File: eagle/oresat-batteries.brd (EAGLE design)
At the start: 99.8 x 94.6 mm, 312 parts, among them J1 J-SAMTEC-TFM-120-X1-XXX-D-RA, J4 ORESAT-DEBUG-CONNECTOR-ALL, Q1 DMP2240UDM, Q10 NTR4101, Q11 PMV45EN, Q12 Si7625DN, Q13 Si7625DN, Q14 NTR4101, Q15 NTR4101, Q16 Si7625DN, Q17 Si7625DN, Q18 Si7625DN, Q19 Si7625DN, Q2 PMV45EN, Q22 PMV45EN, Q23 NTR4101, Q24 PM45VEN, Q25 PM45VEN, Q26 PM45VEN, Q27 PM45VEN, Q28 NTR4101, Q29 PM45VEN, Q3 DMP3050LVT-7, Q30 Si7625DN, Q31 Si7625DN, Q32 NTR4101, Q33 NTR4101, Q34 Si7625DN, Q35 Si7625DN, Q36 Si7625DN, Q37 Si7625DN, Q4 DMP3050LVT-7, Q40 PM45VEN, Q41 NTR4101, Q42 DMP2240UDM, Q43 DMP2240UDM, Q44 PMV45EN, Q45 FDMQ86530L_2-GATES, Q5 PMV45EN, Q6 PM45VEN, Q7 PM45VEN, Q8 PM45VEN, Q9 PM45VEN, U1 MAX7310ATE, U10 LTC4412, U11 LTC4412, U12 MAX17205G, U13 S-8209AAA-T8T1U, U14 S-8209AAA-T8T1U, U15 LTC4412, U16 LTC4412, U17 MAX17205G, U2 MIC842LYC5, U20 TCAN330, U21 STM32F091C, U3 MIC842LYC5, U4 MAX4211FETE, U5 TPS62111RSA, U8 S-8209AAA-T8T1U, U9 S-8209AAA-T8T1U, X3 16MHZ-2.5x2mm

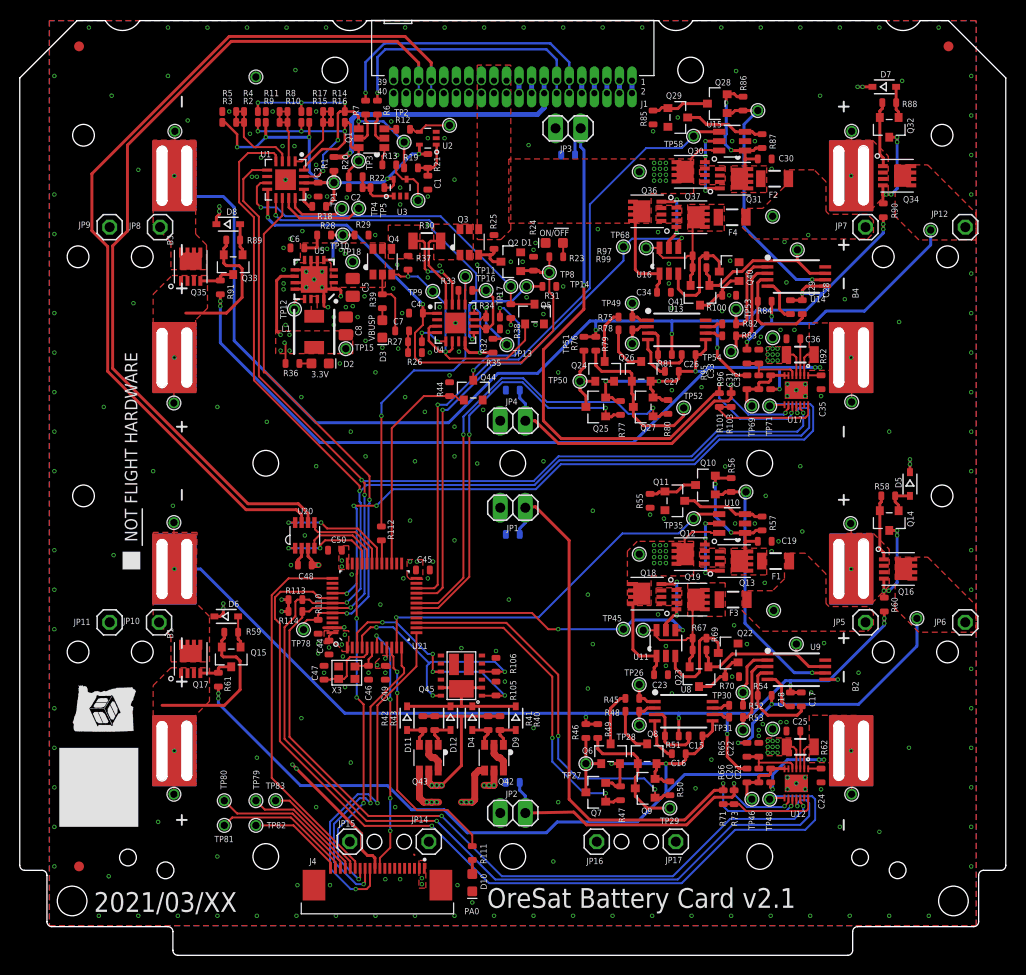
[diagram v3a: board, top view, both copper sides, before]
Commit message: OreSat Battery Card v2.1
- Shrunk fastener foot prints to gain more room.
- Redid DF3 switch layouts to get the jumper wires closer to the switche's mini-contact holes.
- Added fiducials.
- Replaced quad N channel MOSFET with four N channels because the quad pack is unobtainium right now.
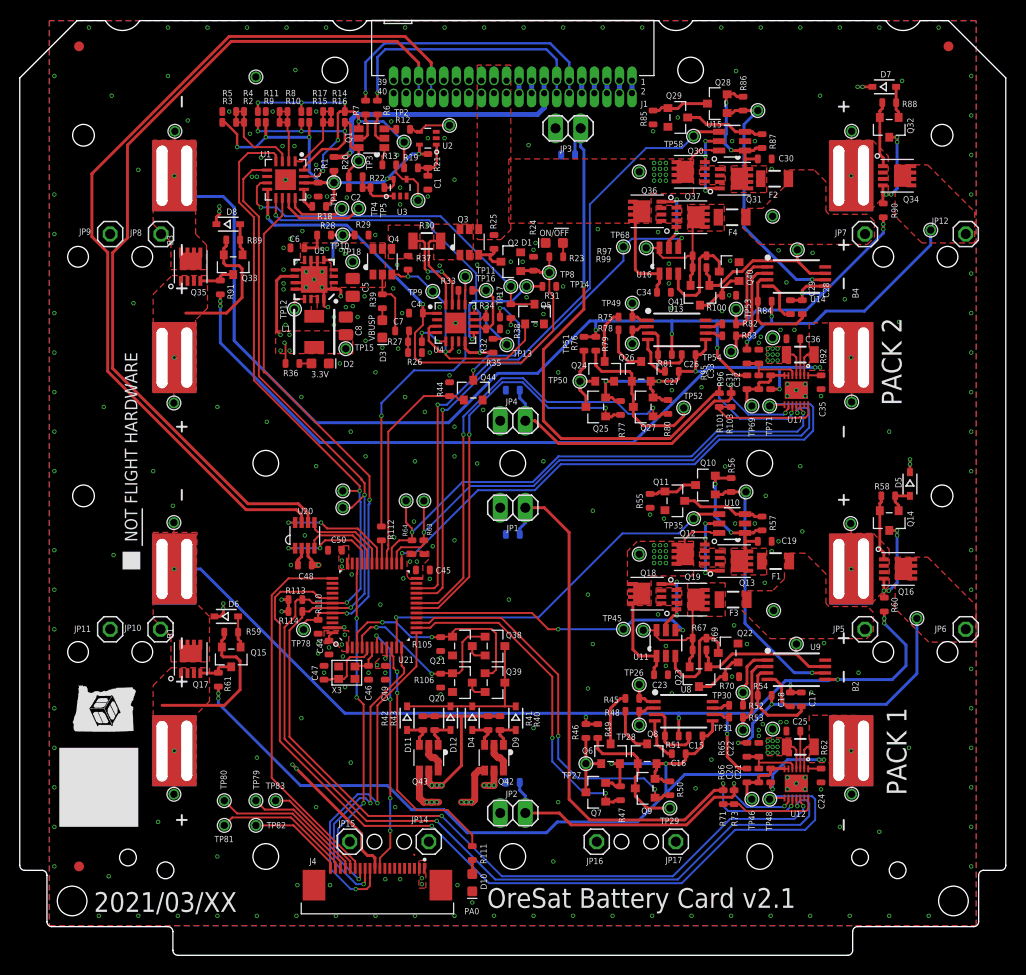
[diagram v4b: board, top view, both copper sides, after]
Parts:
- removed Q45: FDMQ86530L_2-GATES, Q-On_Semiconductor-FDMQ86530L-MOSFET-4-N-CH:FDMQ8203
- added Q20, Q21, Q38, Q39: PMV45EN, Q-MOSFET-NCH-SOT23-3:SOT23-3
- added R63, R64: 4.7k, oresat-rcl:.0603-C-NOSILK
- added TP19, TP20, TP21, TP22: TEST-POINT-LARGE-SQUARE, oresat-misc:1X01
- moved R105 7.18 mm to (42.6, 31.5), turned to 270 degrees
- moved R106 5.82 mm to (42.6, 27.8), turned to 270 degrees
- moved JP10 0.72 mm to (14.2, 33.0)
- moved JP8 0.71 mm to (14.3, 73.0)
- moved JP11 0.70 mm to (9.15, 33.0)
- moved JP9 0.70 mm to (9.15, 73.0)
- moved JP12 0.70 mm to (95.8, 73.0)
- moved JP5 0.70 mm to (85.5, 33.0)
- moved JP6 0.70 mm to (95.8, 33.0)
- moved JP7 0.70 mm to (85.5, 73.0)
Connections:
- new net I2C2_SCL: R63.1, TP19.1, U17.11, U21.26
- new net I2C2_SDA: R64.1, TP20.1, U17.12, U21.27
- new net N$88: Q20.3, Q39.2
- new net N$92: Q21.3, Q38.2
- net 3.3V: now also R63.2, R64.2
- net ALERTA-PK2: now also U21.25; no longer U21.40
- net GND: now also Q20.2, Q21.2; no longer Q45.5, Q45.6, Q45.7, Q45.8
- net HEATER-ON-1: now also Q21.1, Q39.1; no longer Q45.1, Q45.9
- net HEATER-ON-2: now also Q20.1, Q38.1; no longer Q45.12, Q45.4
- net MOARPWR: now also U21.28; no longer U21.27
- net N$64: now also Q38.3, Q39.3; no longer Q45.11, Q45.13, Q45.2
- net PB6/SCL: now also TP21.1; no longer U17.11
- net PB7/SDA: now also TP22.1; no longer U17.12
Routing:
- net I2C2_SCL: track 0.00 -> 56.4 mm, vias 0 -> 2
- net I2C2_SDA: track 0.00 -> 54.5 mm, vias 0 -> 2
- net PB6/SCL: track 193.2 -> 142.2 mm, vias 5 -> 4
- net PB7/SDA: track 181.4 -> 134.8 mm, vias 6 -> 4
- net ALERTA-PK2: track 69.1 -> 56.4 mm, vias 3 -> 1
- net HEATER-ON-2: track 24.8 -> 19.1 mm, vias 3 -> 2
- net INTERCELL-PK1: track 104.1 -> 108.8 mm
- net N$88: track 0.00 -> 2.10 mm
- net N$92: track 0.00 -> 2.10 mm
- net HEATER-ON-1: track 24.2 -> 22.3 mm, vias 4 -> 2
- net VBATT-POS-PK1: track 27.5 -> 29.2 mm
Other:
- board text added: "PACK 1"
- board text added: "PACK 2"

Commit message: Battery v3.0. Might actually work, and with less dropouts.
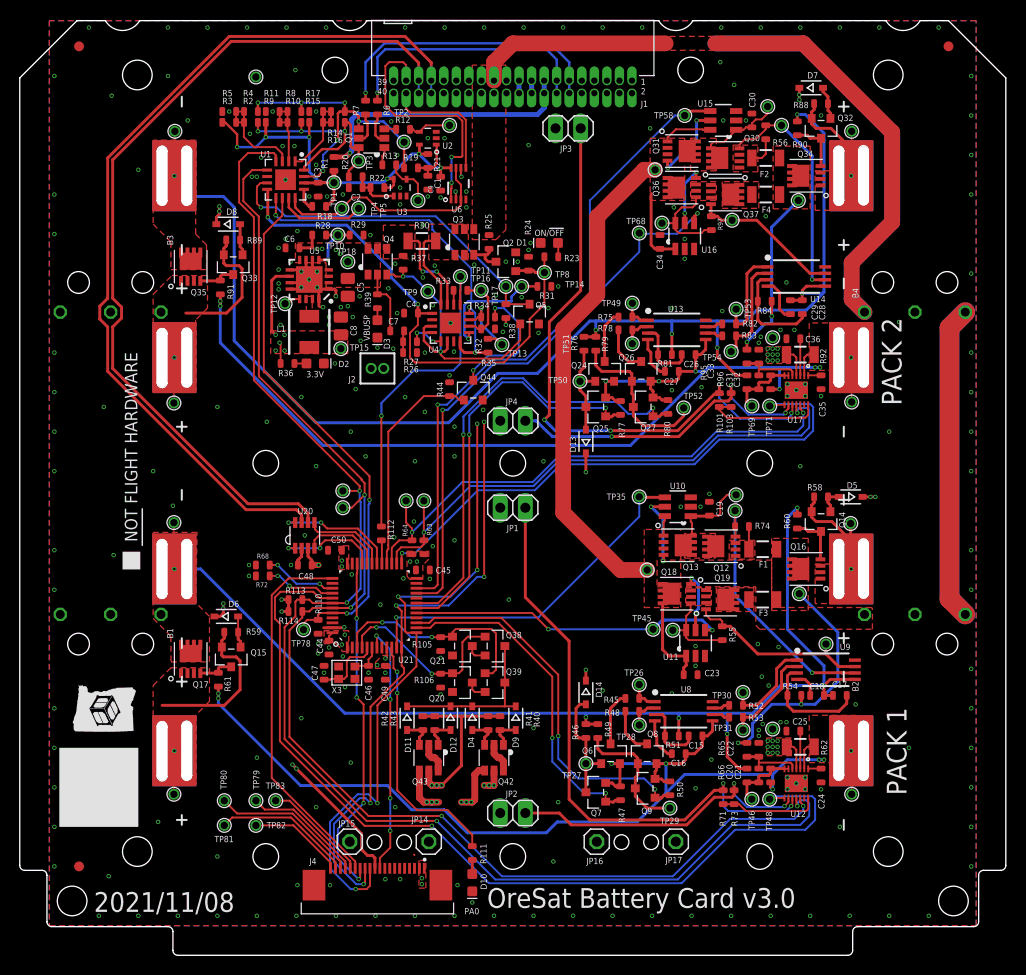
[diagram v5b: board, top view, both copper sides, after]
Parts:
- removed JP10, JP11, JP12, JP5, JP6, JP7, JP8, JP9: (no value), pinhead:1X01
- removed PCB1: ORESAT-CARD-V1.3-BATTERY, oresat-cards:ORESAT-CARD-V1.3-BATTERY
- removed Q10, Q23, Q28, Q41: NTR4101, Q-MOSFET-PCH-SOT23-3:SOT23-3
- removed Q11, Q22: PMV45EN, Q-MOSFET-NCH-SOT23-3:SOT23-3
- removed Q29, Q40: PM45VEN, Q-MOSFET-NCH-SOT23-3:SOT23-3
- removed R100, R57, R67, R69, R70, R85, R86, R87, R99: 100k, oresat-rcl:.0603-C-NOSILK
- removed R102, R104: NP, oresat-rcl:.0603-C-NOSILK
- removed TP37, TP60: TEST-POINT-LARGE-SQUARE, oresat-misc:1X01
- added C9: 100n, oresat-rcl:.0603-C-NOSILK
- added D13, D14: 1N4151WS, D-Generic-silicon-SOD-323:SOD323-R
- added J2: FTS-102-01-X-SJ, J-Samtec-FTS-102-01-1.27mm-th:SAMTEC-FTS-102-01-X-S
- added R68: 10k, oresat-rcl:.0603-C-NOSILK
- added SW1, SW3: OMRON-D2F-5L3-LEFT, SW-Omron-D2F-L3-D-switch:D2F-L3-D-HORIZONTAL-L
- added SW2, SW4: OMRON-D2F-5L3-RIGHT, SW-Omron-D2F-L3-D-switch:D2F-L3-D-HORIZONTAL-R
- added TP23, TP24: TEST-POINT-LARGE-SQUARE, oresat-misc:1X01
- added U$2: (no value), oresat-cards:ORESAT-CARD-V1.3-BATTERY-V3.0
- added U6: TS5A21366DCUR, U-TI-TS5A21366-2xSPST-analog-switch:DCU0008A_N
- R72: value NP -> 10k
- R74: value NP -> 100k
- moved R56 35.9 mm to (75.5, 83.3), turned to 270 degrees
- moved R74 34.8 mm to (73.1, 43.4), flipped to the top
- moved R72 25.6 mm to (24.6, 38.4), flipped to the top
- moved R55 15.3 mm to (71.1, 32.6), turned to 270 degrees
- moved TP61 13.7 mm to (78.8, 76.4)
- moved R60 12.2 mm to (78.7, 43.9), turned to 90 degrees
- moved TP38 12.2 mm to (78.9, 36.6)
- moved R90 12.0 mm to (78.7, 83.7), turned to 90 degrees
- moved Q16 9.30 mm to (79.6, 39.1), turned to 90 degrees
- moved Q34 9.20 mm to (79.6, 78.9), turned to 90 degrees
- moved D7 7.40 mm to (80.1, 87.8)
- moved TP56 7.25 mm to (72.1, 74.4)
- moved Q14 6.90 mm to (81.1, 43.9)
- moved Q32 6.90 mm to (81.1, 83.7)
- moved R88 6.90 mm to (81.1, 86.2)
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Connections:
- removed net N$41: F3.1, Q19.5, Q19.6, Q19.7, Q19.8, Q19.PAD, Q23.2, R67.2, R69.2, TP44.1, U11.6
- removed net N$44: Q18.1, Q18.2, Q18.3, Q19.1, Q19.2, Q19.3
- removed net N$76: Q30.1, Q30.2, Q30.3, Q31.1, Q31.2, Q31.3
- removed net N$81: Q36.1, Q36.2, Q36.3, Q37.1, Q37.2, Q37.3
- removed net N$89: F4.1, Q37.5, Q37.6, Q37.7, Q37.8, Q37.PAD, Q41.2, R97.2, R99.2, TP67.1, U16.6
- removed net N$93: Q28.3, Q29.1, R85.2
- removed net N$94: Q40.3, R97.1, U16.3
- removed net N$95: Q40.1, Q41.3, R100.2
- removed net NLEKJRWER: Q11.3, R57.1, U10.3
- removed net NLEKJRWER2: Q29.3, R87.1, U15.3
- removed net SPARE1: J1.10, J1.9
- removed net SPARE2: J1.7, J1.8
- removed net SPARE3: J1.5, J1.6
- removed net SPARE4: J1.3, J1.4
- removed net SPARE5: J1.1, J1.2
- removed net VBATT-POS-PK1: JP6.1, Q16.5, Q16.6, Q16.7, Q16.8, Q16.PAD, R54.2, R65.2, TP38.1
- removed net VBATT-POS-PK2: JP12.1, Q34.5, Q34.6, Q34.7, Q34.8, Q34.PAD, R84.2, R95.2, TP61.1
- removed net VBATT-SW-PK1: F1.2, F3.2, JP5.1, TP37.1
- removed net VBATT-SW-PK2: F2.2, F4.2, JP7.1, TP60.1
- new net C3-UART-RX: J1.38, U6.5
- new net C3-UART-TX: J1.37, U6.1
- new net INTERSW: SW3.C, SW4.C
- new net N$1: U21.45
- new net N$100: F1.1, Q12.1, Q12.2, Q12.3, R74.1
- new net N$109: Q18.1, Q18.2, Q18.3, Q19.1, Q19.2, Q19.3, R55.2, TP44.1, U11.6
- new net N$13: U21.46
- new net N$54: R68.1, U21.39
- new net N$99: R72.1, U21.40
- new net VBAT: C23.1, C34.1, Q13.1, Q13.2, Q13.3, Q18.5, Q18.6, Q18.7, Q18.8, Q18.PAD, Q31.1, Q31.2, Q31.3, Q36.5, Q36.6, Q36.7, Q36.8, Q36.PAD, SW4.NC, TP36.1, TP59.1, U10.6, U11.1, U15.6, U16.1
- new net VBATT-PK1: F1.2, F3.2, Q16.5, Q16.6, Q16.7, Q16.8, Q16.PAD, R54.2, R65.2, TP38.1
- new net VBATT-PK2: F2.2, F4.2, Q34.5, Q34.6, Q34.7, Q34.8, Q34.PAD, R84.2, R95.2, TP61.1
- net !CHARGE-PK1: now also Q19.4, R55.1; no longer Q23.1, R69.1
- net !CHARGE-PK2: now also Q37.4, R97.1; no longer Q41.1, R99.1
- net !DISCHARGE-PK1: now also Q12.4, R74.2; no longer Q10.1, R56.1
- net !DISCHARGE-PK2: now also Q30.4, R56.1; no longer Q28.1, R86.1
- net !SD: now also D13.C, D14.C, SW1.NO, SW2.NO; no longer JP10.1, JP8.1
- net 3.3V: now also J2.1
- net AIN1-PK1: no longer R74.2
- net AIN1-PK2: no longer R104.2
- net AIN2-PK1: no longer R72.2
- net AIN2-PK2: no longer R102.2
- net GND: now also C9.1, R68.2, R72.2, SW1.C, SW2.C, U15.3, U16.3, U6.4; no longer J1.31, J1.32, J1.37, J1.38, JP11.1, JP9.1, Q11.2, Q22.2, Q29.2, Q40.2, R100.1, R102.1, R104.1, R55.1, R70.1, R72.1, R74.1, R85.1
- net N$22: now also Q36.1, Q36.2, Q36.3, Q37.1, Q37.2, Q37.3, R97.2, TP67.1, U16.6; no longer Q22.3, R67.1, U11.3
- net N$43: no longer Q19.4
- net N$48: now also F3.1, Q19.5, Q19.6, Q19.7, Q19.8, Q19.PAD; no longer Q10.3, Q11.1, R55.2
- net N$51: now also D14.A
- net N$56: now also F2.1, Q30.1, Q30.2, Q30.3, R56.2; no longer Q22.1, Q23.3, R70.2
- net N$60: now also U6.3, U6.7
- net N$74: no longer Q30.4
- net N$8: no longer Q12.4
- net N$80: no longer Q37.4
- net N$9: now also F4.1, Q37.5, Q37.6, Q37.7, Q37.8, Q37.PAD; no longer Q12.1, Q12.2, Q12.3, Q13.1, Q13.2, Q13.3
- net N$91: now also D13.A
- net PA2/USART2_TX: now also U6.6
- net PA3/USART2_RX: now also U6.2
- net VBATT-F-PK1: now also Q12.5, Q12.6, Q12.7, Q12.8, Q12.PAD, TP23.1; no longer F1.1, Q10.2, R56.2, R57.2
- net VBATT-F-PK2: now also Q30.5, Q30.6, Q30.7, Q30.8, Q30.PAD, TP24.1; no longer F2.1, Q28.2, R86.2, R87.2
- net VBUS: now also SW3.NC; no longer C23.1, C34.1, J1.21, J1.22, Q12.5, Q12.6, Q12.7, Q12.8, Q12.PAD, Q18.5, Q18.6, Q18.7, Q18.8, Q18.PAD, Q30.5, Q30.6, Q30.7, Q30.8, Q30.PAD, Q36.5, Q36.6, Q36.7, Q36.8, Q36.PAD, TP36.1, TP59.1, U10.6, U11.1, U15.6, U16.1
- net VPD: now also C9.2, J2.2, U6.8
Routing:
- net INTERSW: track 0.00 -> 95.8 mm
- net VBUS: track 29.6 -> 104.2 mm, vias 24 -> 0
- net VBAT: track 0.00 -> 74.4 mm
- net !SD: track 208.5 -> 278.1 mm, vias 8 -> 10
- net PA2/USART2_TX: track 31.7 -> 91.3 mm, vias 2 -> 6
- net PA3/USART2_RX: track 36.7 -> 94.7 mm, vias 2 -> 6
- net VBATT-POS-PK1: track 29.2 -> 0.00 mm, vias 2 -> 0
- net VBATT-POS-PK2: track 27.2 -> 0.00 mm, vias 2 -> 0
- net VBATT-PK1: track 0.00 -> 25.7 mm, vias 0 -> 2
- net C3-UART-TX: track 0.00 -> 25.4 mm, vias 0 -> 2
- net VBATT-PK2: track 0.00 -> 19.9 mm, vias 0 -> 2
- net N$60: track 6.20 -> 23.4 mm
- net VPD: track 69.9 -> 85.8 mm, vias 6 -> 7
- net N$41: track 13.1 -> 0.00 mm
- net C3-UART-RX: track 0.00 -> 12.9 mm
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- added copper zone on layer 1, net N$100
- added copper zone on layer 1, net N$109
- added copper zone on layer 1, net N$22
- added copper zone on layer 1, net N$48
- added copper zone on layer 1, net N$56
- added copper zone on layer 1, net VBAT
- added copper zone on layer 1, net VBATT-PK1
- added copper zone on layer 1, net VBATT-PK2
- removed copper zone on layer 1, net N$41
- removed copper zone on layer 1, net N$44
- removed copper zone on layer 1, net N$76
- removed copper zone on layer 1, net N$81
- removed copper zone on layer 1, net N$89
- removed copper zone on layer 1, net VBATT-POS-PK1
- removed copper zone on layer 1, net VBATT-POS-PK2
- removed copper zone on layer 1, net VBATT-SW-PK1
- removed copper zone on layer 1, net VBATT-SW-PK2
- removed copper zone on layer 15, net VBUS
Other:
- board text added: "2021/11/08"
- board text added: "OreSat Battery Card v3.0"
- board text removed: "2021/03/XX"
- board text removed: "OreSat Battery Card v2.1"

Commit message: v3.0 sent off to fab! Updated BOM, and committed final changes to card. Lots of small changes, including better power routing, resistors in the UART line to the C3, and as mentioned in an earlier commit, making the charge/discharge switch independent of the ideal diodes.
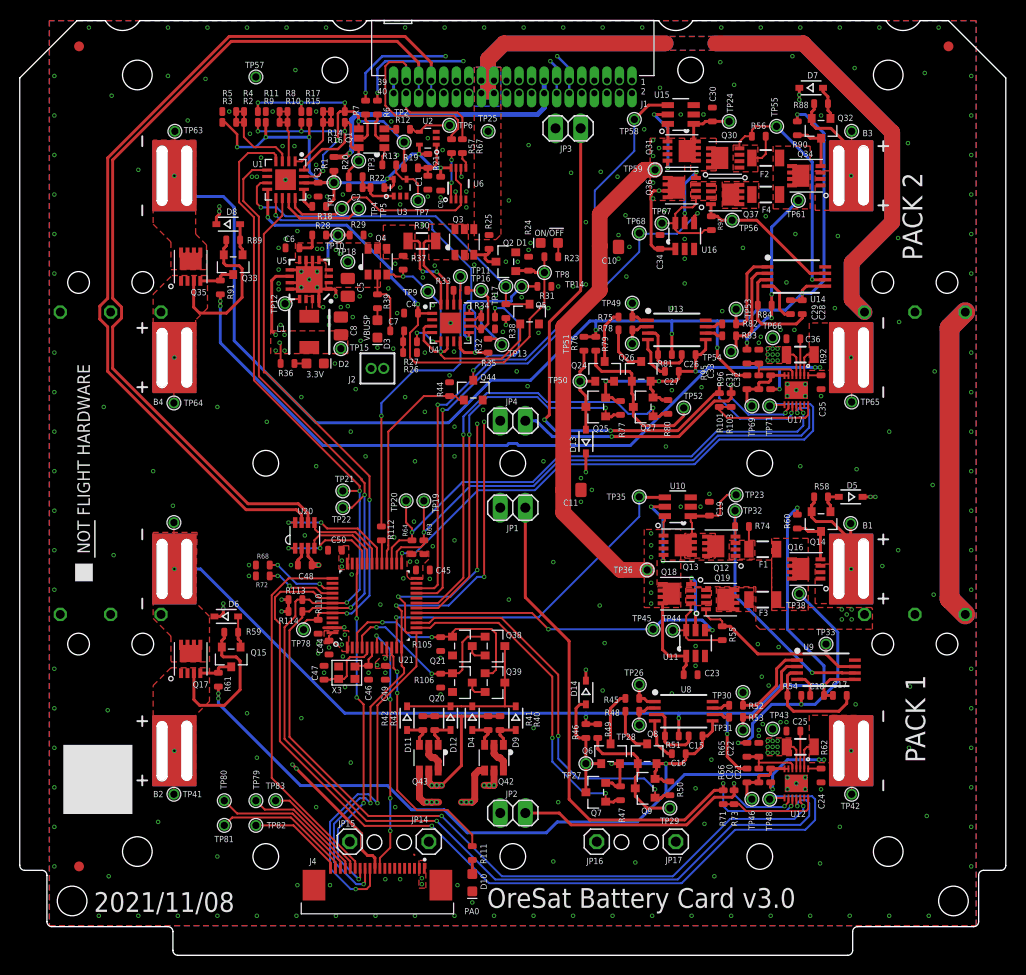
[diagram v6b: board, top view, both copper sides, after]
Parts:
- added C10, C11: 10u, oresat-rcl:.0805-B-NOSILK
- added R57, R67: 10k, oresat-rcl:.0603-C-NOSILK
- added TP25: TEST-POINT-LARGE-SQUARE, oresat-misc:1X01
- R11, R17, R5: value NP -> 10k
- moved SW3 36.6 mm to (90.6, 31.5), turned to 180 degrees
- moved SW4 36.6 mm to (90.6, 68.1), turned to 0 degrees
- moved TP58 5.12 mm to (62.2, 84.6)
- moved U$1 4.95 mm to (7.10, 38.1)
- moved U15 4.34 mm to (66.9, 85.1)
- moved TP24 4.18 mm to (71.8, 84.4)
- moved C30 4.04 mm to (70.1, 85.1)
- moved R56 0.81 mm to (74.8, 82.9), turned to 0 degrees
- moved TP55 0.51 mm to (76.6, 83.9)
- moved R84 0.40 mm to (75.4, 65.8)
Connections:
- removed net CAN2_H: J1.17, J1.18
- removed net CAN2_L: J1.19, J1.20
- net C3-UART-RX: now also R67.2; no longer U6.5
- net C3-UART-TX: now also R57.2; no longer U6.1
- net GND: now also C10.2, C11.2, U10.3, U11.3
- net INTERSW: now also SW3.NC, SW4.NC; no longer SW3.C, SW4.C
- net N$1: now also R57.1, U6.1; no longer U21.45
- net N$13: now also R67.1, U6.5; no longer U21.46
- net VBAT: now also C10.1, C11.1, SW3.C; no longer SW4.NC
- net VBUS: now also SW4.C, TP25.1; no longer SW3.NC
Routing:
- net VBAT: track 74.4 -> 147.5 mm, vias 0 -> 17
- net !SD: track 278.1 -> 303.8 mm
- net VBUS: track 104.2 -> 128.0 mm
- net C3-UART-TX: track 25.4 -> 18.1 mm, vias 2 -> 0
- net N$1: track 0.00 -> 4.72 mm, vias 0 -> 2
- net C3-UART-RX: track 12.9 -> 9.83 mm
- net INTERCELL-PK2: track 134.6 -> 131.8 mm
- net VBATT-F-PK2: track 8.35 -> 5.56 mm
- net VBATT-PK2: track 19.9 -> 17.5 mm, vias 2 -> 3
- net OPD_SCL: track 26.7 -> 24.5 mm, vias 1 -> 3
- net N$85: track 18.4 -> 20.5 mm
- net OPD_SDA: track 29.2 -> 27.1 mm, vias 1 -> 3
- net DCHG-STAT-OC-PK2: track 66.0 -> 64.2 mm
- net N$13: track 0.00 -> 1.64 mm
- net CAN2_L: track 1.27 -> 0.00 mm
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- added copper zone on layer 15, net VBAT
- added copper zone on layer 16, net VBUS
